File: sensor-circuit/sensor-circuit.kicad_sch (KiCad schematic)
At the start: 5 parts

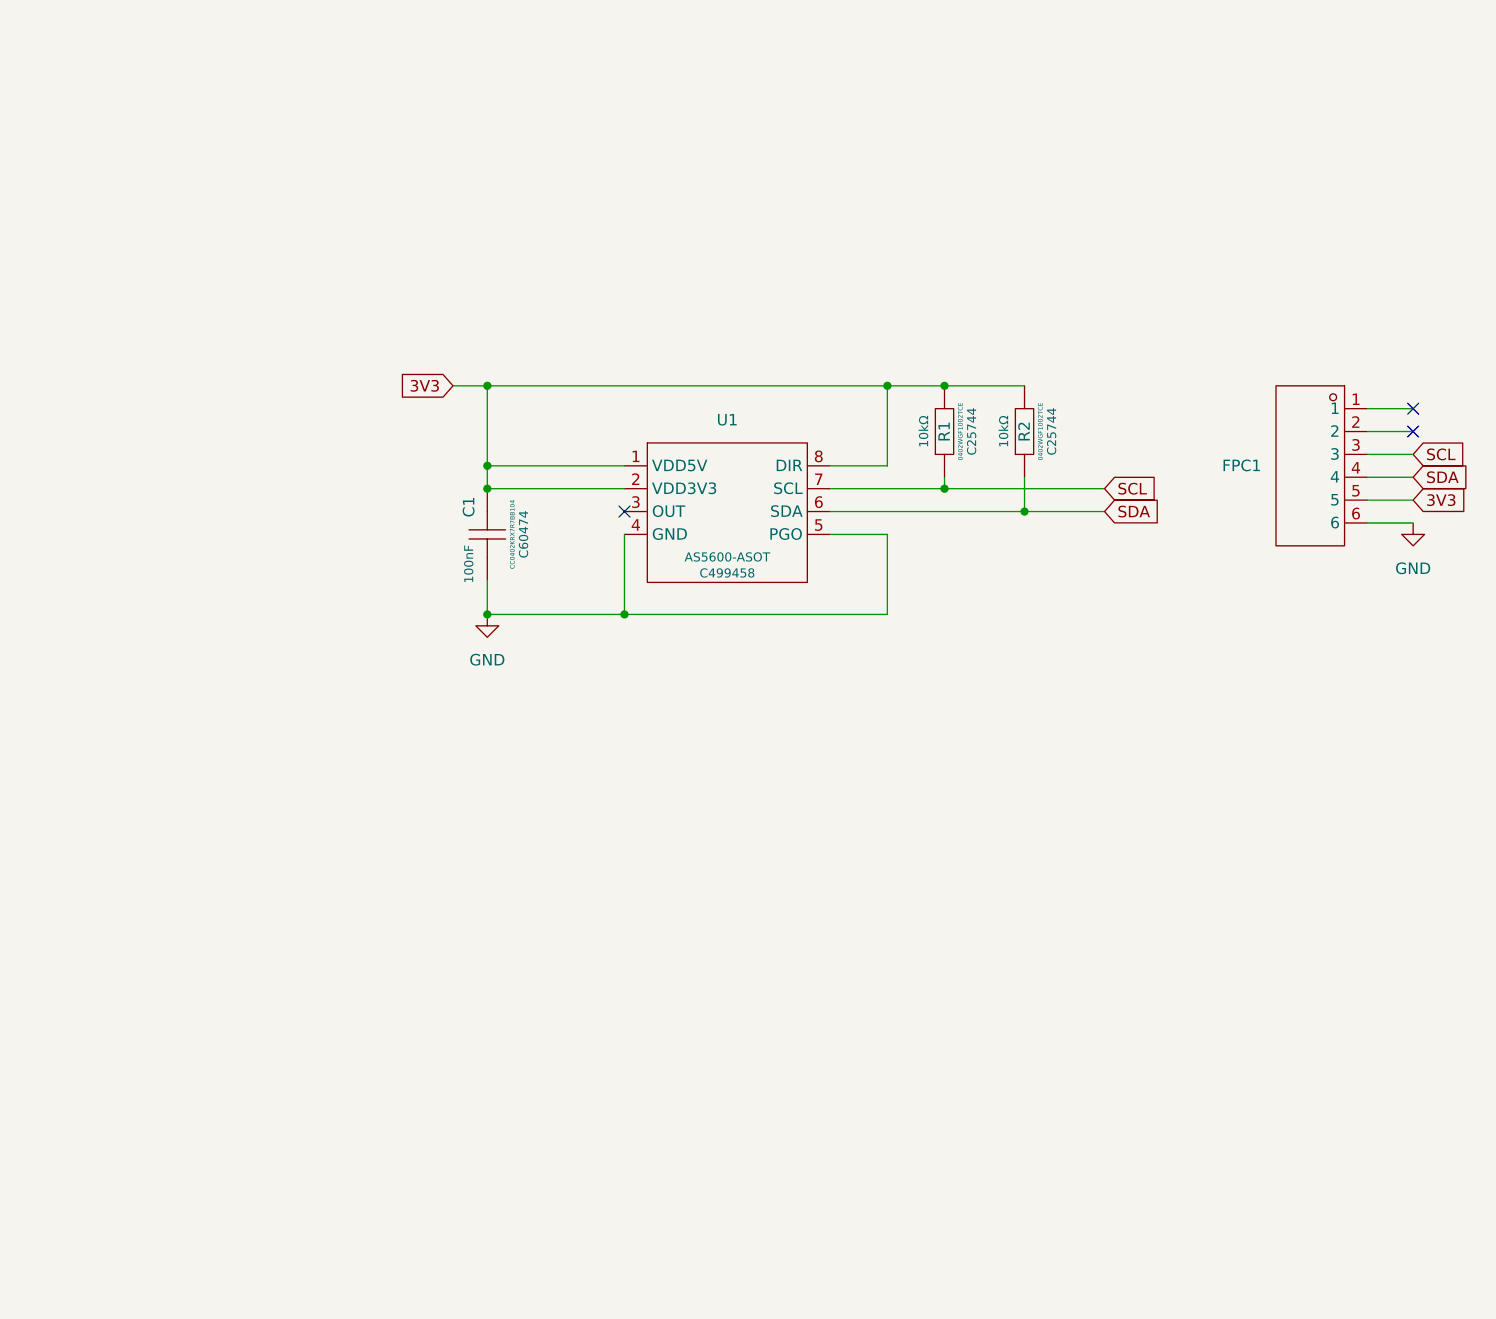
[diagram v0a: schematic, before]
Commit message: Fix sensors panel for production.
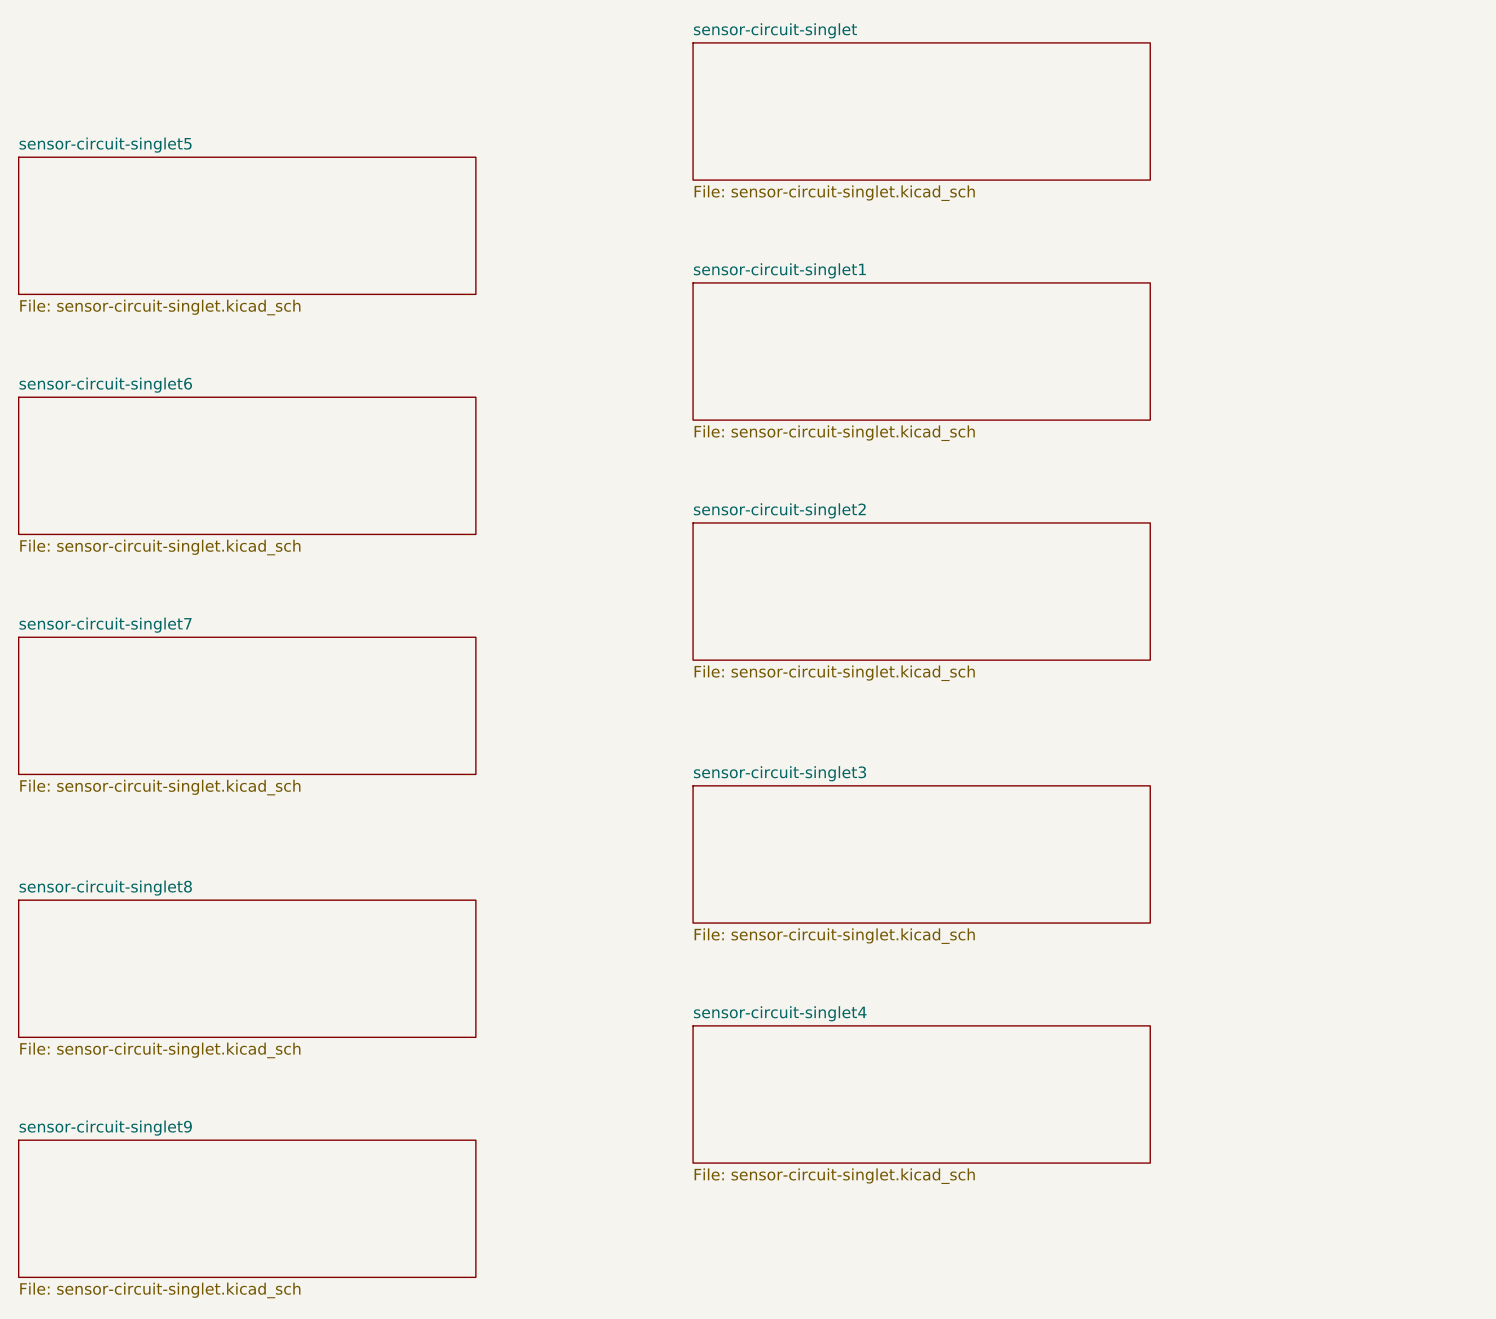
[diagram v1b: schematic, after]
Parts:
- removed C1: 100nF, Library:C0402, symbol Library:CC0402KRX7R7BB104 Capacitor 100nF
- removed FPC1: ~, Library:FPC-6P-P0.50-Pattern, symbol Library:FPC-05F-6PH20 Pattern 6P 0.5mm spacing
- removed R1, R2: 10kΩ, Library:R0402, symbol Library:0402WGF1002TCE Resistor 10kΩ
- removed U1: ~, Library:SOIC-8_L5.0-W4.0-P1.27-LS6.0-BL, symbol Library:AS5600-ASOT Magnetic rotary encoder
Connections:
- no-connect marks 3 -> 0
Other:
- added sheet sensor-circuit-singlet (sensor-circuit-singlet.kicad_sch)
- added sheet sensor-circuit-singlet1 (sensor-circuit-singlet.kicad_sch)
- added sheet sensor-circuit-singlet2 (sensor-circuit-singlet.kicad_sch)
- added sheet sensor-circuit-singlet3 (sensor-circuit-singlet.kicad_sch)
- added sheet sensor-circuit-singlet4 (sensor-circuit-singlet.kicad_sch)
- added sheet sensor-circuit-singlet5 (sensor-circuit-singlet.kicad_sch)
- added sheet sensor-circuit-singlet6 (sensor-circuit-singlet.kicad_sch)
- added sheet sensor-circuit-singlet7 (sensor-circuit-singlet.kicad_sch)
- added sheet sensor-circuit-singlet8 (sensor-circuit-singlet.kicad_sch)
- added sheet sensor-circuit-singlet9 (sensor-circuit-singlet.kicad_sch)
